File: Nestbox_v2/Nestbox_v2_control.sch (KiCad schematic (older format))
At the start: 20 parts, among them P1 RX/TX, P2 TST/RST, P3 VDD/GND, SW1 SMD-BUTTON_2P-3.0X2.5X1.2+0.4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, U1 MSP430FR5969, Y1 Crystal

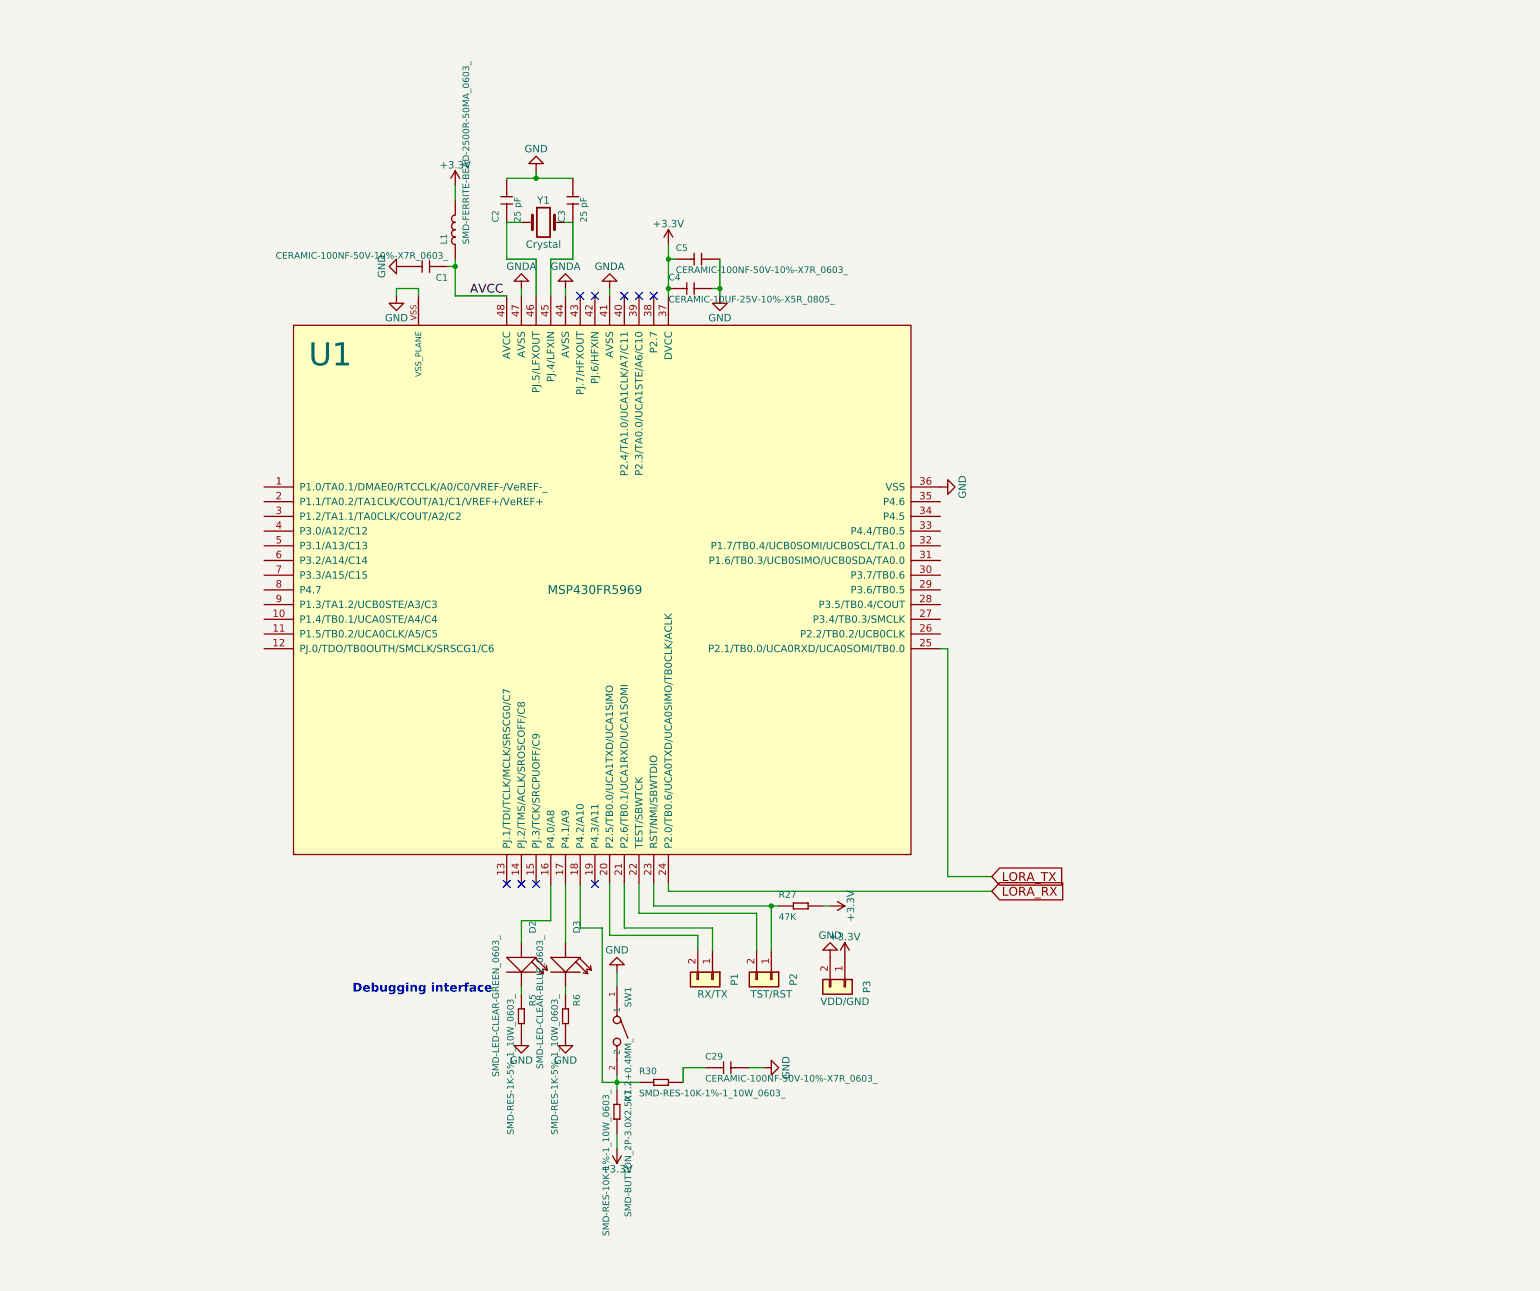
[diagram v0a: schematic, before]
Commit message: Connects global signals to MSP430
- Connect SPI signals for SD-Card
- Connect RFID signals for MLX
- Connect ADC signals for housekeeping
- Connect Lightbarrier signals
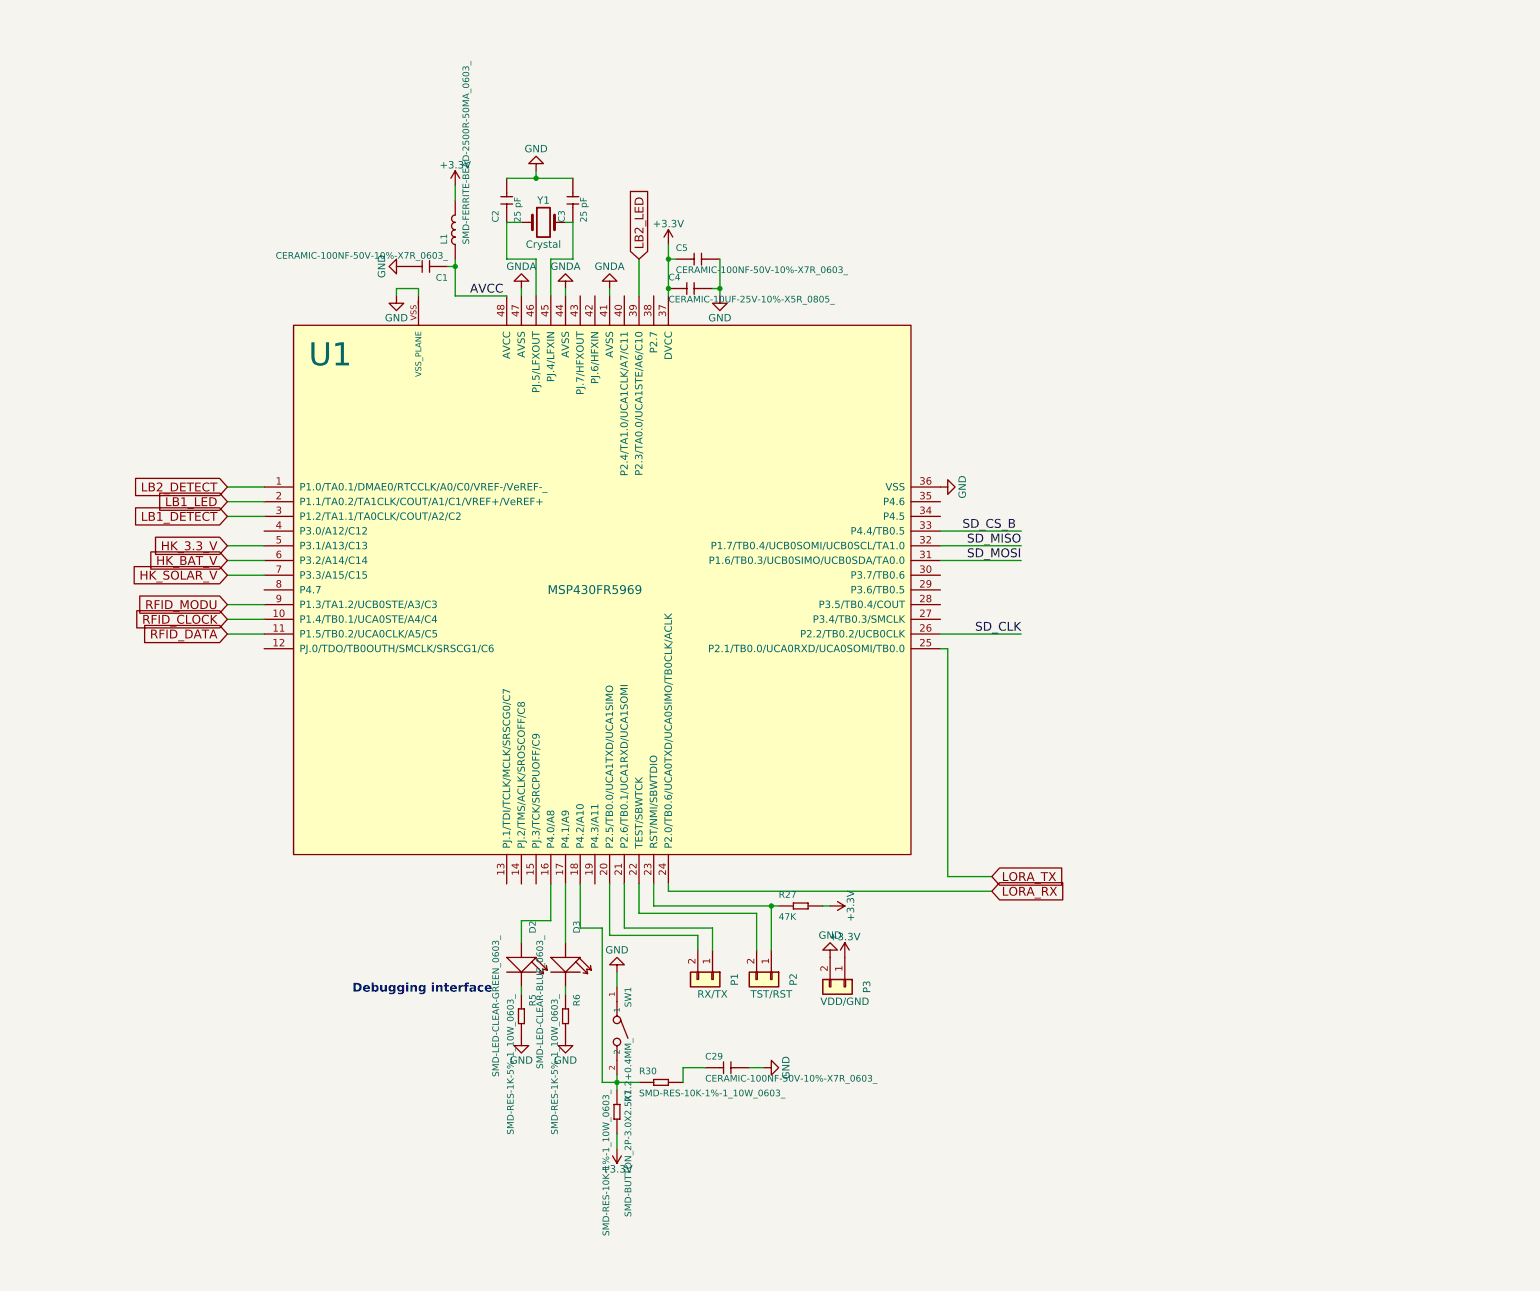
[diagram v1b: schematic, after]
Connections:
- net LB2_DETECT: now reaches U1.1 (P1.0/TA0.1/DMAE0/RTCCLK/A0/C0/VREF-/VeREF-_)
- net RFID_CLOCK: now reaches U1.10 (P1.4/TB0.1/UCA0STE/A4/C4)
- net RFID_DATA: now reaches U1.11 (P1.5/TB0.2/UCA0CLK/A5/C5)
- net LB1_LED: now reaches U1.2 (P1.1/TA0.2/TA1CLK/COUT/A1/C1/VREF+/VeREF+)
- net SD_CLK: now reaches U1.26 (P2.2/TB0.2/UCB0CLK)
- net LB1_DETECT: now reaches U1.3 (P1.2/TA1.1/TA0CLK/COUT/A2/C2)
- net SD_MOSI: now reaches U1.31 (P1.6/TB0.3/UCB0SIMO/UCB0SDA/TA0.0)
- net SD_MISO: now reaches U1.32 (P1.7/TB0.4/UCB0SOMI/UCB0SCL/TA1.0)
- net SD_CS_B: now reaches U1.33 (P4.4/TB0.5)
- net LB2_LED: now reaches U1.39 (P2.3/TA0.0/UCA1STE/A6/C10)
- net HK_3.3_V: now reaches U1.5 (P3.1/A13/C13)
- net HK_BAT_V: now reaches U1.6 (P3.2/A14/C14)
- net HK_SOLAR_V: now reaches U1.7 (P3.3/A15/C15)
- net RFID_MODU: now reaches U1.9 (P1.3/TA1.2/UCB0STE/A3/C3)
- no-connect marks 9 -> 0
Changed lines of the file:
@@
 Text GLabel 7200 5850 2    60   Input ~ 0
 LORA_RX
-NoConn ~ 4500 5800
-NoConn ~ 4100 5800
-NoConn ~ 4000 5800
-NoConn ~ 3900 5800
-NoConn ~ 4400 1800
-NoConn ~ 4500 1800
-NoConn ~ 4700 1800
-NoConn ~ 4800 1800
-NoConn ~ 4900 1800
 Text Label 3650 1800 0    60   ~ 0
 AVCC
@@
 Wire Wire Line
 	5550 7050 5650 7050
+Wire Wire Line
+	6850 3500 7400 3500
+Wire Wire Line
+	6850 3600 7400 3600
+Text Label 7400 3500 2    60   ~ 0
+SD_MISO
+Text Label 7400 3600 2    60   ~ 0
+SD_MOSI
+Wire Wire Line
+	6850 4100 7400 4100
+Text Label 7400 4100 2    60   ~ 0
+SD_CLK
+Text GLabel 2000 3900 0    60   Input ~ 0
+RFID_MODU
+Text GLabel 2000 4100 0    60   Input ~ 0
+RFID_DATA
+Text GLabel 2000 4000 0    60   Input ~ 0
+RFID_CLOCK
+Wire Wire Line
+	2000 3900 2250 3900
+Wire Wire Line
+	2250 4000 2000 4000
+Wire Wire Line
+	2000 4100 2250 4100
+Text GLabel 2000 3500 0    60   Input ~ 0
+HK_3.3_V
+Text GLabel 2000 3600 0    60   Input ~ 0
+HK_BAT_V
+Text GLabel 2000 3700 0    60   Input ~ 0
+HK_SOLAR_V
+Wire Wire Line
+	2000 3500 2250 3500
+Wire Wire Line
+	2250 3600 2000 3600
+Wire Wire Line
+	2000 3700 2250 3700
+Wire Wire Line
+	6850 3400 7400 3400
+Text Label 7000 3400 0    60   ~ 0
+SD_CS_B
+Text GLabel 2000 3100 0    60   Input ~ 0
+LB2_DETECT
+Text GLabel 2000 3200 0    60   Input ~ 0
+LB1_LED
+Text GLabel 2000 3300 0    60   Input ~ 0
+LB1_DETECT
+Wire Wire Line
+	2000 3100 2250 3100
+Wire Wire Line
+	2250 3200 2000 3200
+Wire Wire Line
+	2000 3300 2250 3300
+Text GLabel 4800 1550 1    60   Input ~ 0
+LB2_LED
+Wire Wire Line
+	4800 1550 4800 1800
 $EndSCHEMATC

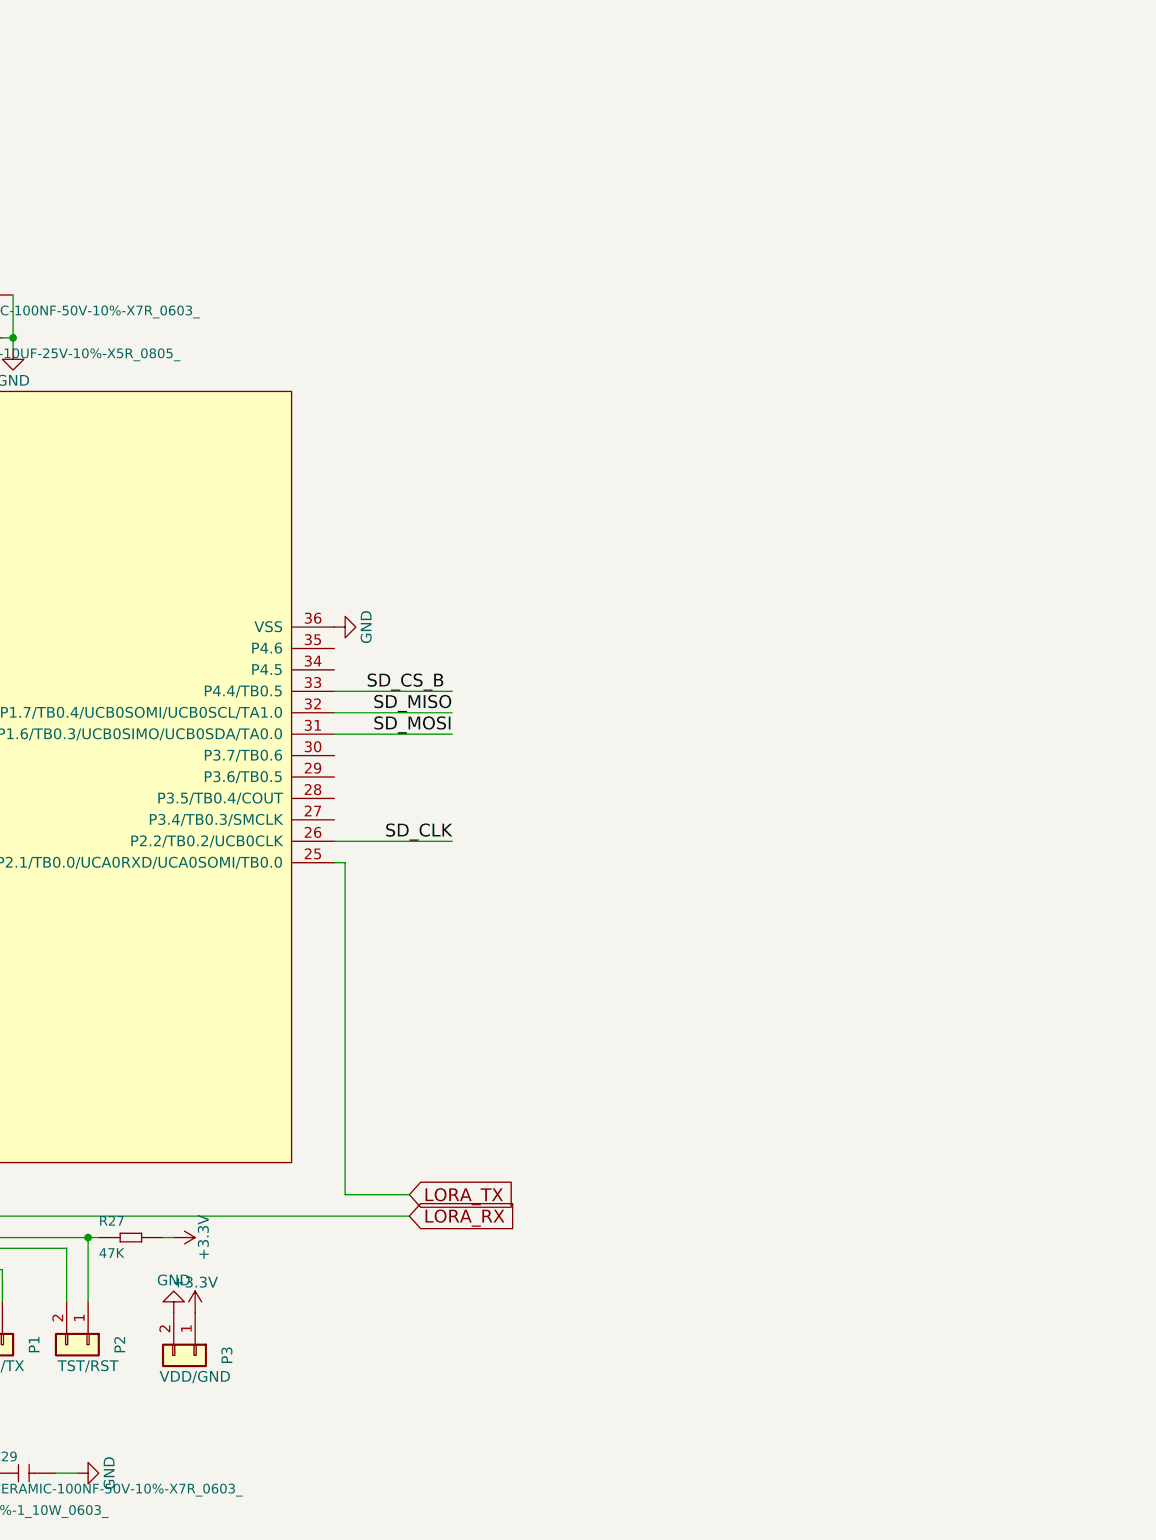
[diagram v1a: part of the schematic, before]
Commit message: Adds SD card to Control schematic
SD card schematic symbol has been added and connected.
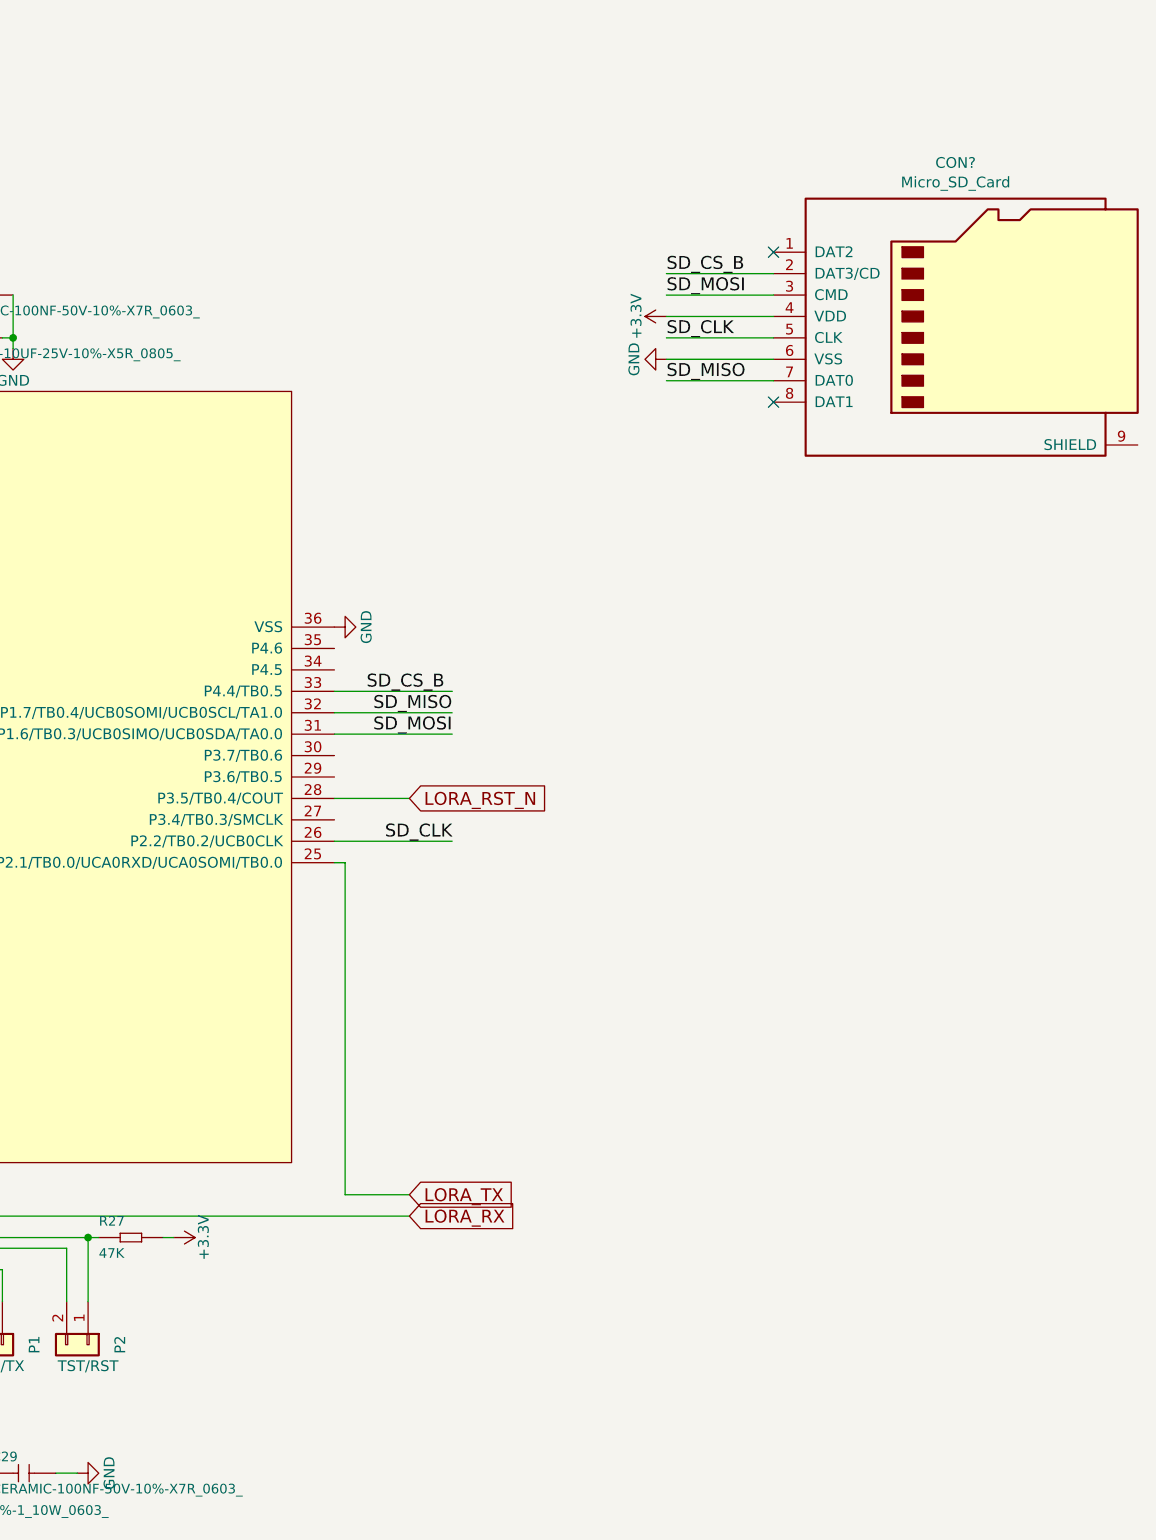
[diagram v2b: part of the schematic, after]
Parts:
- removed P3: VDD/GND, Socket_Strips:Socket_Strip_Straight_1x02, symbol Conn_01x02
- added CON?: Micro_SD_Card, symbol Micro_SD_Card
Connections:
- net +3V3: now also CON?.4 (VDD)
- net GND: now also CON?.6 (VSS)
- net SD_CLK: now also CON?.5 (CLK)
- net SD_CS_B: now also CON?.2 (DAT3/CD)
- net SD_MISO: now also CON?.7 (DAT0)
- net SD_MOSI: now also CON?.3 (CMD)
- net LORA_RST_N: now reaches U1.28 (P3.5/TB0.4/COUT)
- no-connect marks 0 -> 2
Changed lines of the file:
@@
 	0    1    1    0
-$EndComp
-$Comp
-L Conn_01x02 P3
-U 1 1 587BBB5F
-P 6200 6500
-AR Path="/587BBB5F" Ref="P3"  Part="1"
-AR Path="/59EF7F04/587BBB5F" Ref="P3"  Part="1"
-F 0 "P3" H 6200 6650 50  0000 C CNN
-F 1 "VDD/GND" V 6300 6500 50  0000 C CNN
-F 2 "Socket_Strips:Socket_Strip_Straight_1x02" H 6200 6500 50  0001 C CNN
-F 3 "" H 6200 6500 50  0000 C CNN
-F 4 "" H 6200 6500 50  0001 C CNN "MPN"
-F 5 "" H 6200 6500 50  0001 C CNN "SKU"
-F 6 "" H 6200 6500 50  0001 C CNN "MouserLink"
-	1    6200 6500
-	0    1    1    0
-$EndComp
-$Comp
-L +3.3V #PWR020
-U 1 1 587BBBBA
-P 6200 6300
-F 0 "#PWR020" H 6200 6150 50  0001 C CNN
-F 1 "+3.3V" H 6200 6440 50  0000 C CNN
-F 2 "" H 6200 6300 50  0000 C CNN
-F 3 "" H 6200 6300 50  0000 C CNN
-	1    6200 6300
-	1    0    0    -1
-$EndComp
-$Comp
-L GND #PWR021
-U 1 1 587BBC10
-P 6100 6300
-F 0 "#PWR021" H 6100 6050 50  0001 C CNN
-F 1 "GND" H 6100 6150 50  0000 C CNN
-F 2 "" H 6100 6300 50  0000 C CNN
-F 3 "" H 6100 6300 50  0000 C CNN
-	1    6100 6300
-	-1   0    0    1
 $EndComp
 Text GLabel 7200 5850 2    60   Input ~ 0
@@
 Wire Wire Line
 	4800 1550 4800 1800
+Text GLabel 7200 3900 2    60   Input ~ 0
+LORA_RST_N
+Wire Wire Line
+	6850 3900 7200 3900
+$Comp
+L Micro_SD_Card CON?
+U 1 1 59FCE4BD
+P 9800 1650
+F 0 "CON?" H 9750 2367 50  0000 C CNN
+F 1 "Micro_SD_Card" H 9750 2276 50  0000 C CNN
+F 2 "" H 10950 1950 50  0000 C CNN
+F 3 "" H 9800 1650 50  0000 C CNN
+	1    9800 1650
+	1    0    0    -1
+$EndComp
+NoConn ~ 8900 1350
+NoConn ~ 8900 2050
+Wire Wire Line
+	8900 1450 8400 1450
+Text Label 8400 1450 0    60   ~ 0
+SD_CS_B
+Wire Wire Line
+	8900 1550 8400 1550
+Wire Wire Line
+	8900 1650 8400 1650
+Wire Wire Line
+	8900 1750 8400 1750
+Wire Wire Line
+	8900 1850 8400 1850
+Wire Wire Line
+	8900 1950 8400 1950
+Text Label 8400 1550 0    60   ~ 0
+SD_MOSI
+$Comp
+L +3.3V #PWR?
+U 1 1 59FCECA7
+P 8400 1650
+F 0 "#PWR?" H 8400 1500 50  0001 C CNN
+F 1 "+3.3V" H 8400 1790 50  0000 C CNN
+F 2 "" H 8400 1650 50  0000 C CNN
+F 3 "" H 8400 1650 50  0000 C CNN
+	1    8400 1650
+	0    -1   -1   0
+$EndComp
+$Comp
+L GND #PWR?
+U 1 1 59FCED84
+P 8400 1850
+F 0 "#PWR?" H 8400 1600 50  0001 C CNN
+F 1 "GND" H 8400 1700 50  0000 C CNN
+F 2 "" H 8400 1850 50  0000 C CNN
+F 3 "" H 8400 1850 50  0000 C CNN
+	1    8400 1850
+	0    1    1    0
+$EndComp
+Text Label 8400 1750 0    60   ~ 0
+SD_CLK
+Text Label 8400 1950 0    60   ~ 0
+SD_MISO
 $EndSCHEMATC
